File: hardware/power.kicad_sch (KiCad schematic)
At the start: 68 parts, among them J1 B2B-XH-A, J2 USB4105-GF-A, J3 PRPC001DAAN-RC, J4 PRPC001DAAN-RC, J5 61300111121, J6 61300111121, J7 61300111121, J8 PRPC001DAAN-RC, J9 PRPC001DAAN-RC, Q1 IRLML6401TRPBF, Q2 DMN2005, Q3 DMN2005, U1 BQ29728DSER, U2 LM66200DRLR, U3 MCP73833T-FCI/MF, U4 TPS63020DSJR, U5 MAX17048G+T10

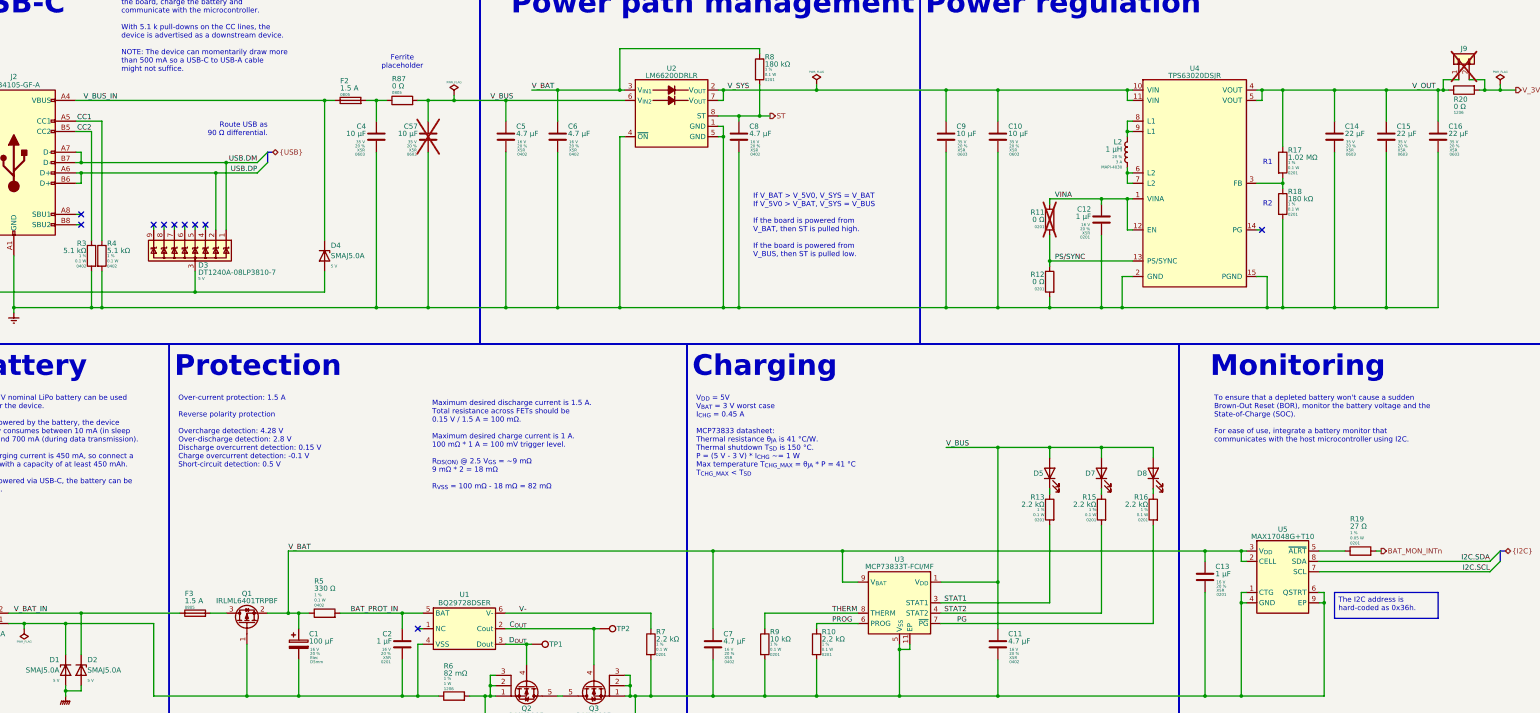
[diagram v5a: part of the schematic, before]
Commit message: HW: Redo MDM UART
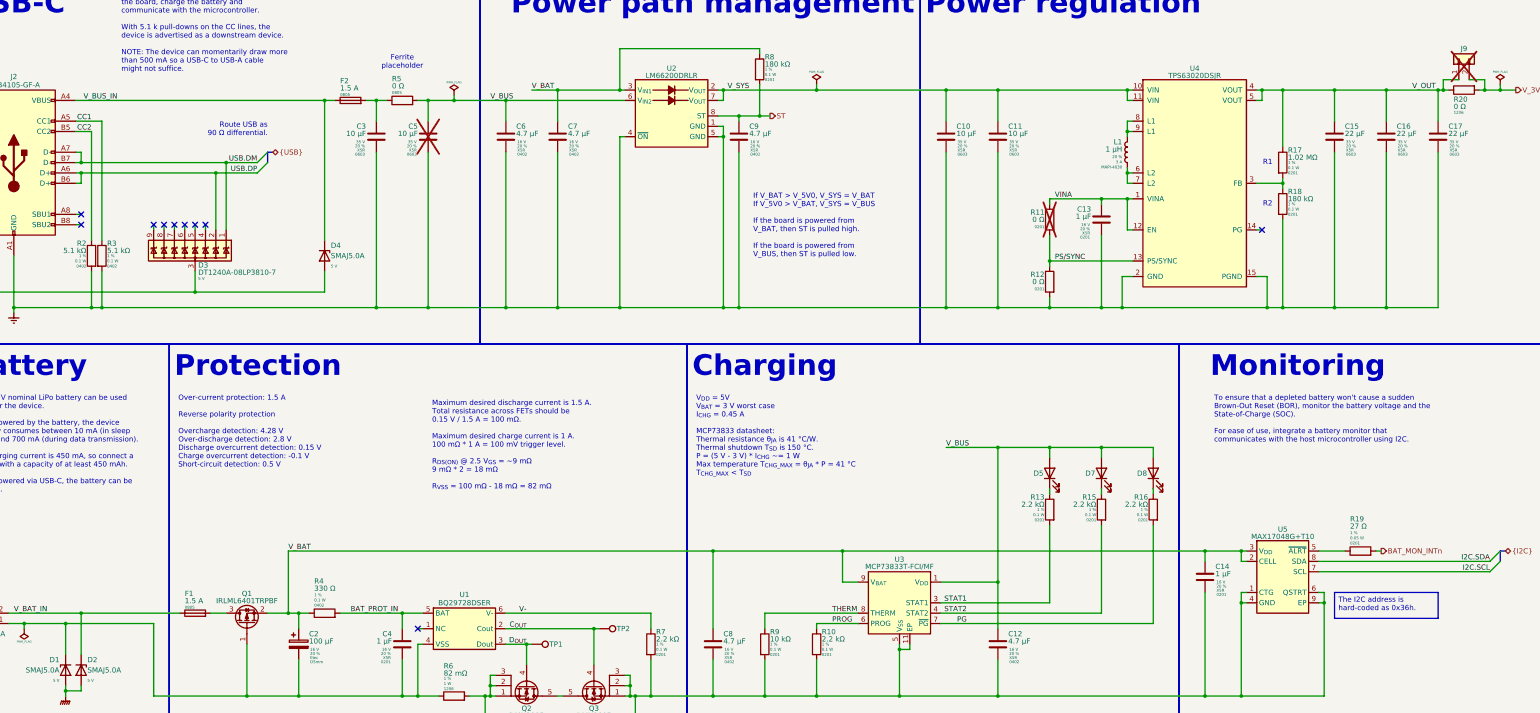
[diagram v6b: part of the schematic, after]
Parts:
- renumbered C9 to C10, C10 to C11, C11 to C12, C12 to C13, C13 to C14, C14 to C15, C15 to C16, C16 to C17, C1 to C2, C4 to C3, C2 to C4, C57 to C5, C5 to C6, C6 to C7, C7 to C8, C8 to C9, F3 to F1, L2 to L1, R3 to R2, R4 to R3, R5 to R4, R87 to R5
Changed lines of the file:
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@@
 		(in_pos_files yes)
 		(dnp no)
-		(property "Reference" "R3"
+		(property "Reference" "R2"
 			(at 43.18 102.362 0)
 			(show_name no)
@@
 			(project "iida_devkit"
 				(path "/b12a6e25-97fb-4aba-bc96-af8db389bb9a/5e1bb3da-9ec5-412a-a6e9-5701708c7ef6"
-					(reference "R3")
+					(reference "R2")
 					(unit 1)
 				)
@@
 		(in_pos_files yes)
 		(dnp no)
-		(property "Reference" "C5"
+		(property "Reference" "C6"
 			(at 148.59 73.66 0)
 			(show_name no)
@@
 			(project "iida_devkit"
 				(path "/b12a6e25-97fb-4aba-bc96-af8db389bb9a/5e1bb3da-9ec5-412a-a6e9-5701708c7ef6"
-					(reference "C5")
+					(reference "C6")
 					(unit 1)
 				)
@@
 		(in_pos_files yes)
 		(dnp no)
-		(property "Reference" "C12"
+		(property "Reference" "C13"
 			(at 289.56 93.98 0)
 			(show_name no)
@@
 			(project "iida_devkit"
 				(path "/b12a6e25-97fb-4aba-bc96-af8db389bb9a/5e1bb3da-9ec5-412a-a6e9-5701708c7ef6"
-					(reference "C12")
+					(reference "C13")
 					(unit 1)
 				)
@@
 		(in_pos_files yes)
 		(dnp no)
-		(property "Reference" "F3"
+		(property "Reference" "F1"
 			(at 67.31 188.976 90)
 			(show_name no)
@@
 			(project "iida_devkit"
 				(path "/b12a6e25-97fb-4aba-bc96-af8db389bb9a/5e1bb3da-9ec5-412a-a6e9-5701708c7ef6"
-					(reference "F3")
+					(reference "F1")
 					(unit 1)
 				)
@@
 		(in_pos_files yes)
 		(dnp no)
-		(property "Reference" "C11"
+		(property "Reference" "C12"
 			(at 269.24 198.12 0)
 			(show_name no)
@@
 			(project "iida_devkit"
 				(path "/b12a6e25-97fb-4aba-bc96-af8db389bb9a/5e1bb3da-9ec5-412a-a6e9-5701708c7ef6"
-					(reference "C11")
+					(reference "C12")
 					(unit 1)
 				)
@@
 		(in_pos_files yes)
 		(dnp no)
-		(property "Reference" "R4"
+		(property "Reference" "R3"
 			(at 48.26 102.362 0)
 			(show_name no)
@@
 			(project "iida_devkit"
 				(path "/b12a6e25-97fb-4aba-bc96-af8db389bb9a/5e1bb3da-9ec5-412a-a6e9-5701708c7ef6"
-					(reference "R4")
+					(reference "R3")
 					(unit 1)
 				)
@@
 		(in_pos_files yes)
 		(dnp no)
-		(property "Reference" "C4"
+		(property "Reference" "C3"
 			(at 111.76 73.66 0)
 			(show_name no)
@@
 			(project "iida_devkit"
 				(path "/b12a6e25-97fb-4aba-bc96-af8db389bb9a/5e1bb3da-9ec5-412a-a6e9-5701708c7ef6"
-					(reference "C4")
+					(reference "C3")
 					(unit 1)
 				)
@@
 		(in_pos_files yes)
 		(dnp no)
-		(property "Reference" "R87"
+		(property "Reference" "R5"
 			(at 118.11 62.738 90)
 			(show_name no)
@@
 			(project "iida_devkit"
 				(path "/b12a6e25-97fb-4aba-bc96-af8db389bb9a/5e1bb3da-9ec5-412a-a6e9-5701708c7ef6"
-					(reference "R87")
+					(reference "R5")
 					(unit 1)
 				)
@@
 		(in_pos_files yes)
 		(dnp no)
-		(property "Reference" "C8"
+		(property "Reference" "C9"
 			(at 205.74 73.66 0)
 			(show_name no)
@@
 			(project "iida_devkit"
 				(path "/b12a6e25-97fb-4aba-bc96-af8db389bb9a/5e1bb3da-9ec5-412a-a6e9-5701708c7ef6"
-					(reference "C8")
+					(reference "C9")
 					(unit 1)
 				)
@@
 		(in_pos_files yes)
 		(dnp no)
-		(property "Reference" "C16"
+		(property "Reference" "C17"
 			(at 377.19 73.66 0)
 			(show_name no)
@@
 			(project "iida_devkit"
 				(path "/b12a6e25-97fb-4aba-bc96-af8db389bb9a/5e1bb3da-9ec5-412a-a6e9-5701708c7ef6"
-					(reference "C16")
+					(reference "C17")
 					(unit 1)
 				)
@@
 		(in_pos_files yes)
 		(dnp no)
-		(property "Reference" "C1"
+		(property "Reference" "C2"
 			(at 97.79 198.12 0)
 			(show_name no)
@@
 			(project "iida_devkit"
 				(path "/b12a6e25-97fb-4aba-bc96-af8db389bb9a/5e1bb3da-9ec5-412a-a6e9-5701708c7ef6"
-					(reference "C1")
+					(reference "C2")
 					(unit 1)
 				)
@@
 		(in_pos_files yes)
 		(dnp no)
-		(property "Reference" "C9"
+		(property "Reference" "C10"
 			(at 256.54 73.66 0)
 			(show_name no)
@@
 			(project "iida_devkit"
 				(path "/b12a6e25-97fb-4aba-bc96-af8db389bb9a/5e1bb3da-9ec5-412a-a6e9-5701708c7ef6"
-					(reference "C9")
+					(reference "C10")
 					(unit 1)
 				)
@@
 		(in_pos_files yes)
 		(dnp no)
-		(property "Reference" "C13"
+		(property "Reference" "C14"
 			(at 320.04 181.61 0)
 			(show_name no)
@@
 			(project "iida_devkit"
 				(path "/b12a6e25-97fb-4aba-bc96-af8db389bb9a/5e1bb3da-9ec5-412a-a6e9-5701708c7ef6"
-					(reference "C13")
+					(reference "C14")
 					(unit 1)
 				)
@@
 		(in_pos_files yes)
 		(dnp no)
-		(property "Reference" "R5"
+		(property "Reference" "R4"
 			(at 99.06 185.928 90)
 			(show_name no)
@@
 			(project "iida_devkit"
 				(path "/b12a6e25-97fb-4aba-bc96-af8db389bb9a/5e1bb3da-9ec5-412a-a6e9-5701708c7ef6"
-					(reference "R5")
+					(reference "R4")
 					(unit 1)
 				)
@@
 		(in_pos_files yes)
 		(dnp no)
-		(property "Reference" "C14"
+		(property "Reference" "C15"
 			(at 351.79 73.66 0)
 			(show_name no)
@@
 			(project "iida_devkit"
 				(path "/b12a6e25-97fb-4aba-bc96-af8db389bb9a/5e1bb3da-9ec5-412a-a6e9-5701708c7ef6"
-					(reference "C14")
+					(reference "C15")
 					(unit 1)
 				)
@@
 		(in_pos_files yes)
 		(dnp no)
-		(property "Reference" "C7"
+		(property "Reference" "C8"
 			(at 199.39 198.12 0)
 			(show_name no)
@@
 			(project "iida_devkit"
 				(path "/b12a6e25-97fb-4aba-bc96-af8db389bb9a/5e1bb3da-9ec5-412a-a6e9-5701708c7ef6"
-					(reference "C7")
+					(reference "C8")
 					(unit 1)
 				)
@@
 		(in_pos_files yes)
 		(dnp no)
-		(property "Reference" "C2"
+		(property "Reference" "C4"
 			(at 118.11 198.12 0)
 			(show_name no)
@@
 			(project "iida_devkit"
 				(path "/b12a6e25-97fb-4aba-bc96-af8db389bb9a/5e1bb3da-9ec5-412a-a6e9-5701708c7ef6"
-					(reference "C2")
+					(reference "C4")
 					(unit 1)
 				)
@@
 		(in_pos_files yes)
 		(dnp yes)
-		(property "Reference" "C57"
+		(property "Reference" "C5"
 			(at 124.46 73.66 0)
 			(show_name no)
@@
 			(project "iida_devkit"
 				(path "/b12a6e25-97fb-4aba-bc96-af8db389bb9a/5e1bb3da-9ec5-412a-a6e9-5701708c7ef6"
-					(reference "C57")
+					(reference "C5")
 					(unit 1)
 				)
@@
 		(in_pos_files yes)
 		(dnp no)
-		(property "Reference" "C10"
+		(property "Reference" "C11"
 			(at 269.24 73.66 0)
 			(show_name no)
@@
 			(project "iida_devkit"
 				(path "/b12a6e25-97fb-4aba-bc96-af8db389bb9a/5e1bb3da-9ec5-412a-a6e9-5701708c7ef6"
-					(reference "C10")
+					(reference "C11")
 					(unit 1)
 				)
@@
 		(in_pos_files yes)
 		(dnp no)
-		(property "Reference" "C6"
+		(property "Reference" "C7"
 			(at 161.29 73.66 0)
 			(show_name no)
@@
 			(project "iida_devkit"
 				(path "/b12a6e25-97fb-4aba-bc96-af8db389bb9a/5e1bb3da-9ec5-412a-a6e9-5701708c7ef6"
-					(reference "C6")
+					(reference "C7")
 					(unit 1)
 				)
@@
 		(in_pos_files yes)
 		(dnp no)
-		(property "Reference" "L2"
+		(property "Reference" "L1"
 			(at 297.18 78.232 0)
 			(show_name no)
@@
 			(project "iida_devkit"
 				(path "/b12a6e25-97fb-4aba-bc96-af8db389bb9a/5e1bb3da-9ec5-412a-a6e9-5701708c7ef6"
-					(reference "L2")
+					(reference "L1")
 					(unit 1)
 				)
@@
 		(in_pos_files yes)
 		(dnp no)
-		(property "Reference" "C15"
+		(property "Reference" "C16"
 			(at 364.49 73.66 0)
 			(show_name no)
@@
 			(project "iida_devkit"
 				(path "/b12a6e25-97fb-4aba-bc96-af8db389bb9a/5e1bb3da-9ec5-412a-a6e9-5701708c7ef6"
-					(reference "C15")
+					(reference "C16")
 					(unit 1)
 				)

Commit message: HW: BAT_DETn -> USB_DET
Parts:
- R219: renamed from R20; footprint Resistor_SMD:R_1206_3216Metric -> Resistor_SMD:R_0805_2012Metric; Digi-Key Part Number RMCF1206ZT0R00CT-ND -> (none); MPN RMCF1206ZT0R00 -> (none); Manufacturer Stackpole Electronics Inc -> (none); Size 1206 -> 0805
- renumbered C2 to C201, C3 to C202, C4 to C203, C5 to C204, C6 to C205, C7 to C206, C8 to C207, C9 to C208, C10 to C209, C11 to C210, C12 to C211, C13 to C212, C14 to C213, C15 to C214, C16 to C215, C17 to C216, D1 to D201, D2 to D202, D3 to D203, D4 to D204, D5 to D205, D6 to D206, D7 to D207, D8 to D208, F1 to F201, F2 to F202, J1 to J201, J2 to J202, J3 to J203, J4 to J204, J5 to J205, J6 to J206, J7 to J207, J8 to J208, J9 to J209, L1 to L201, Q1 to Q201, Q2 to Q202, Q3 to Q203, R2 to R201, R3 to R202, R4 to R203, R5 to R204, R6 to R205, R7 to R206, R8 to R207, R9 to R208, R10 to R209, R11 to R210, R12 to R211, R13 to R212, R14 to R213, R15 to R214, R16 to R215, R17 to R216, R18 to R217, R19 to R218, TP1 to TP201, TP2 to TP202, TP3 to TP203, TP4 to TP204, TP5 to TP205, U1 to U201, U2 to U202, U3 to U203, U4 to U204, U5 to U205

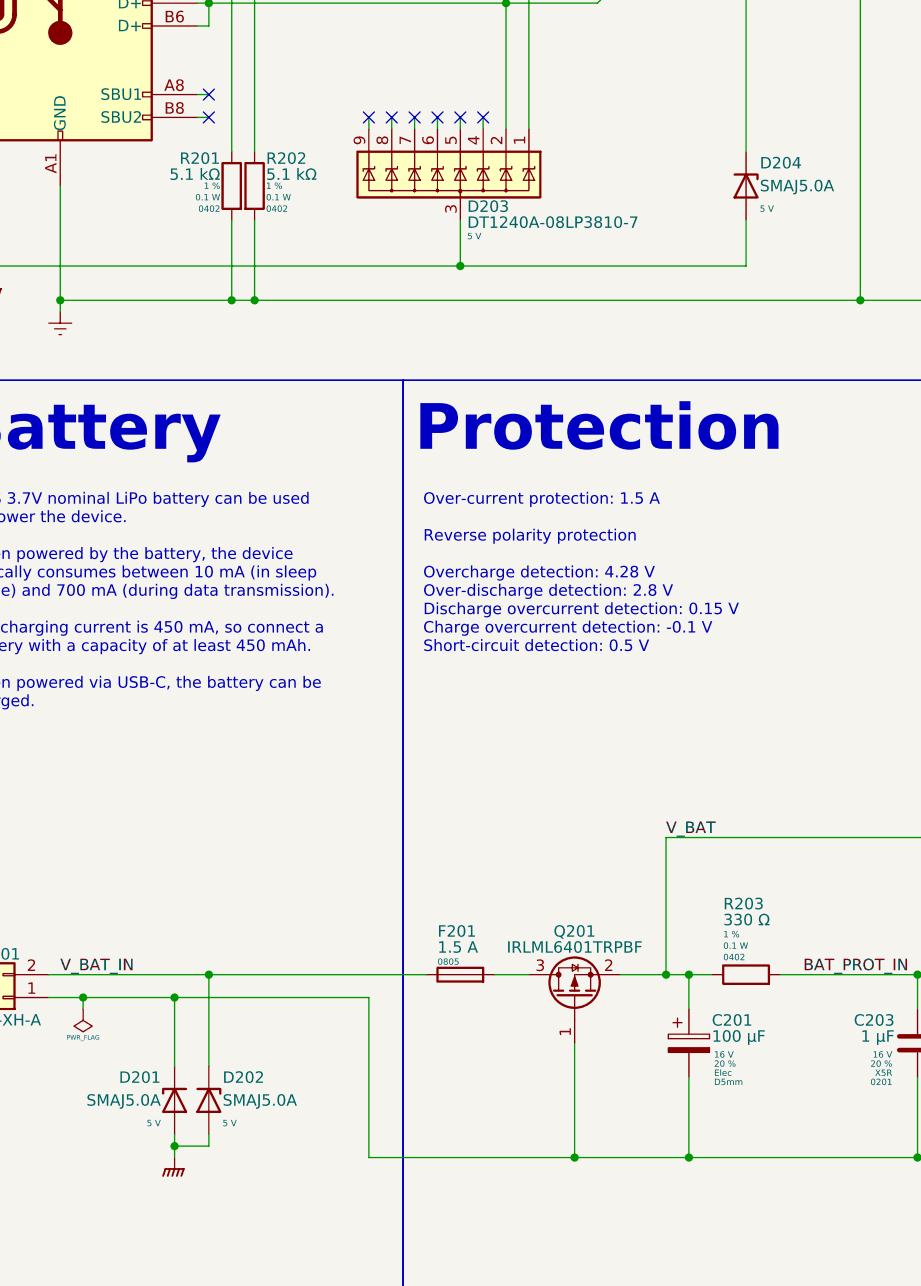
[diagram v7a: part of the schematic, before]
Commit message: HW: Refine Antennas
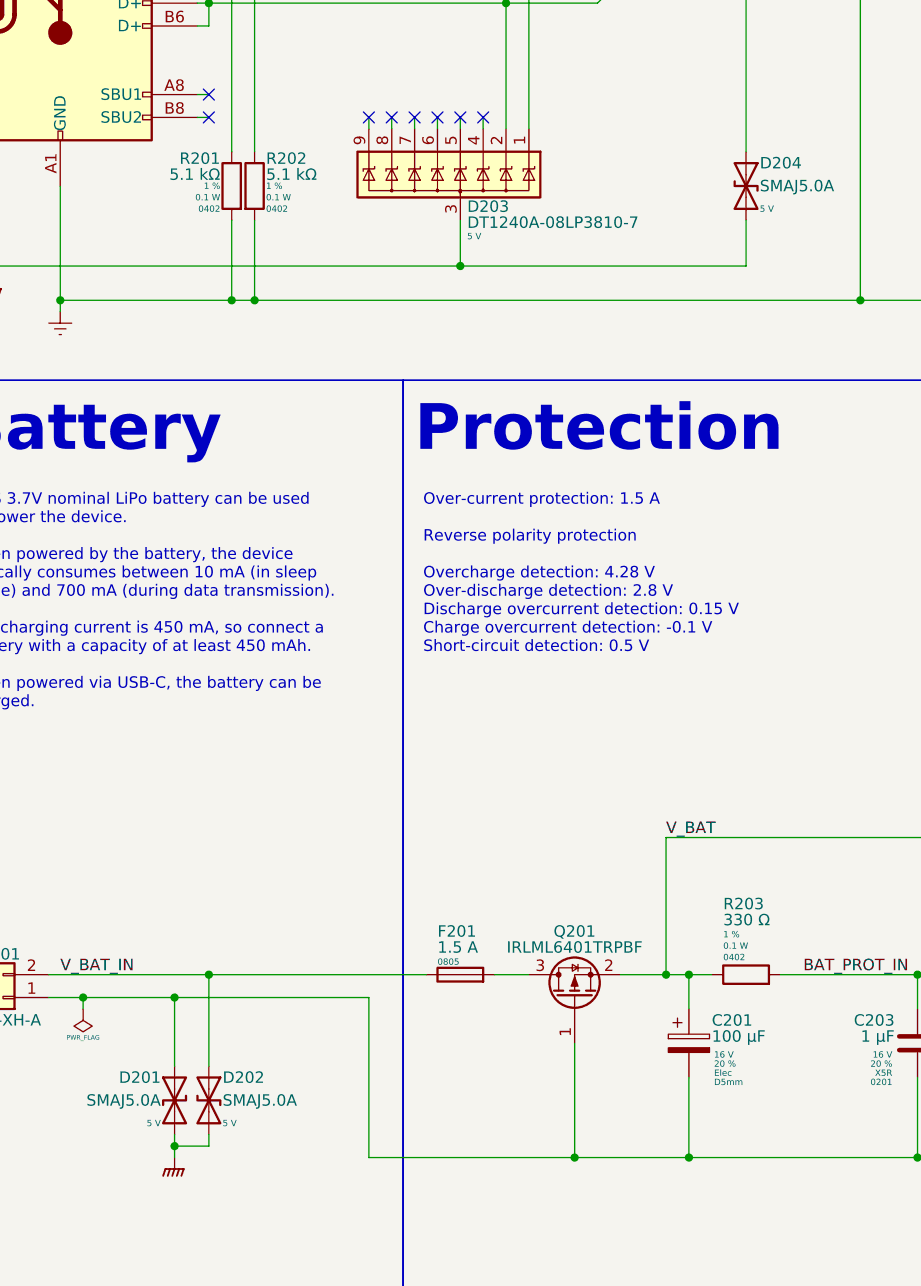
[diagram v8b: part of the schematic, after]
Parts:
- D201, D202, D204: symbol Device:D_Zener -> Device:D_TVS
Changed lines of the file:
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@@
 	)
 	(symbol
-		(lib_id "Device:D_Zener")
+		(lib_id "Device:D_TVS")
 		(at 41.91 207.01 270)
 		(unit 1)
@@
 			)
 		)
-		(property "Description" "9.2V Clamp 43.5A Ipp Tvs Diode Surface Mount SMA"
+		(property "Description" "Bidirectional transient-voltage-suppression diode"
 			(at 41.91 207.01 0)
 			(hide yes)
@@
 	)
 	(symbol
-		(lib_id "Device:D_Zener")
+		(lib_id "Device:D_TVS")
 		(at 101.6 105.41 270)
 		(unit 1)
@@
 			)
 		)
-		(property "Description" "9.2V Clamp 43.5A Ipp Tvs Diode Surface Mount SMA"
+		(property "Description" "Bidirectional transient-voltage-suppression diode"
 			(at 101.6 105.41 0)
 			(hide yes)
@@
 	)
 	(symbol
-		(lib_id "Device:D_Zener")
+		(lib_id "Device:D_TVS")
 		(at 38.1 207.01 90)
 		(mirror x)
@@
 			)
 		)
-		(property "Description" "9.2V Clamp 43.5A Ipp Tvs Diode Surface Mount SMA"
+		(property "Description" "Bidirectional transient-voltage-suppression diode"
 			(at 38.1 207.01 0)
 			(hide yes)
